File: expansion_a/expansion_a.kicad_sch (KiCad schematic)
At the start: 3 parts, among them J101 Conn_01x08, U101 74HC373, U102 74HC595

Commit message: Expander Final II
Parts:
- U102: footprint Package_SO:STC_SOP-16_3.9x9.9mm_P1.27mm -> Package_SO:SOIC-16W_5.3x10.2mm_P1.27mm; LCSC C18164493 -> C5947
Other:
- sheet Output 1 ports: added set(3V3); removed set(+5V)
- sheet Output 2 ports: added set(3V3); removed set(+5V)
- sheet Output 3 ports: added set(3V3); removed set(+5V)
- sheet Output 4 ports: added set(3V3); removed set(+5V)
- sheet Output 5 ports: added set(3V3); removed set(+5V)
- sheet Output 6 ports: added set(3V3); removed set(+5V)
- sheet Output 7 ports: added set(3V3); removed set(+5V)
- sheet Output 8 ports: added set(3V3); removed set(+5V)
- title: (none) -> Expansion Board A
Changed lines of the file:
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@@
 	(generator_version "8.0")
 	(paper "A4")
+	(title_block
+		(title "Expansion Board A")
+		(date "2025-01-01")
+		(rev "1")
+	)
 	(junction
 		(at 247.65 25.4)
@@
 			)
 		)
-		(property "Footprint" "Package_SO:STC_SOP-16_3.9x9.9mm_P1.27mm"
+		(property "Footprint" "Package_SO:SOIC-16W_5.3x10.2mm_P1.27mm"
 			(at 160.02 71.12 0)
 			(effects
@@
 			)
 		)
-		(property "LCSC" "C18164493"
+		(property "LCSC" "C5947"
 			(at 160.02 71.12 0)
 			(effects
@@
 			)
 		)
-		(pin "set(+5V)" passive
-			(at 210.82 58.42 180)
+		(pin "output" passive
+			(at 223.52 60.96 0)
 			(effects
 				(font
 					(size 1.27 1.27)
 				)
-				(justify left)
+				(justify right)
 			)
 		)
-		(pin "output" passive
-			(at 223.52 60.96 0)
+		(pin "GND" passive
+			(at 210.82 63.5 180)
 			(effects
 				(font
 					(size 1.27 1.27)
 				)
-				(justify right)
+				(justify left)
 			)
 		)
-		(pin "GND" passive
-			(at 210.82 63.5 180)
+		(pin "set(3V3)" passive
+			(at 210.82 58.42 180)
 			(effects
 				(font
@@
 			)
 		)
-		(pin "set(+5V)" passive
-			(at 257.81 33.02 180)
+		(pin "output" passive
+			(at 270.51 35.56 0)
 			(effects
 				(font
 					(size 1.27 1.27)
 				)
-				(justify left)
+				(justify right)
 			)
 		)
-		(pin "output" passive
-			(at 270.51 35.56 0)
+		(pin "GND" passive
+			(at 257.81 38.1 180)
 			(effects
 				(font
 					(size 1.27 1.27)
 				)
-				(justify right)
+				(justify left)
 			)
 		)
-		(pin "GND" passive
-			(at 257.81 38.1 180)
+		(pin "set(3V3)" passive
+			(at 257.81 33.02 180)
 			(effects
 				(font
@@
 			)
 		)
-		(pin "set(+5V)" passive
-			(at 210.82 33.02 180)
+		(pin "output" passive
+			(at 223.52 35.56 0)
 			(effects
 				(font
 					(size 1.27 1.27)
 				)
-				(justify left)
+				(justify right)
 			)
 		)
-		(pin "output" passive
-			(at 223.52 35.56 0)
+		(pin "GND" passive
+			(at 210.82 38.1 180)
 			(effects
 				(font
 					(size 1.27 1.27)
 				)
-				(justify right)
+				(justify left)
 			)
 		)
-		(pin "GND" passive
-			(at 210.82 38.1 180)
+		(pin "set(3V3)" passive
+			(at 210.82 33.02 180)
 			(effects
 				(font
@@
 			)
 		)
-		(pin "set(+5V)" passive
-			(at 257.81 58.42 180)
+		(pin "output" passive
+			(at 270.51 60.96 0)
 			(effects
 				(font
 					(size 1.27 1.27)
 				)
-				(justify left)
+				(justify right)
 			)
 		)
-		(pin "output" passive
-			(at 270.51 60.96 0)
+		(pin "GND" passive
+			(at 257.81 63.5 180)
 			(effects
 				(font
 					(size 1.27 1.27)
 				)
-				(justify right)
+				(justify left)
 			)
 		)
-		(pin "GND" passive
-			(at 257.81 63.5 180)
+		(pin "set(3V3)" passive
+			(at 257.81 58.42 180)
 			(effects
 				(font
@@
 			)
 		)
-		(pin "set(+5V)" passive
-			(at 210.82 82.55 180)
+		(pin "output" passive
+			(at 223.52 85.09 0)
 			(effects
 				(font
 					(size 1.27 1.27)
 				)
-				(justify left)
+				(justify right)
 			)
 		)
-		(pin "output" passive
-			(at 223.52 85.09 0)
+		(pin "GND" passive
+			(at 210.82 87.63 180)
 			(effects
 				(font
 					(size 1.27 1.27)
 				)
-				(justify right)
+				(justify left)
 			)
 		)
-		(pin "GND" passive
-			(at 210.82 87.63 180)
+		(pin "set(3V3)" passive
+			(at 210.82 82.55 180)
 			(effects
 				(font
@@
 			)
 		)
-		(pin "set(+5V)" passive
-			(at 257.81 107.95 180)
+		(pin "output" passive
+			(at 270.51 110.49 0)
 			(effects
 				(font
 					(size 1.27 1.27)
 				)
-				(justify left)
+				(justify right)
 			)
 		)
-		(pin "output" passive
-			(at 270.51 110.49 0)
+		(pin "GND" passive
+			(at 257.81 113.03 180)
 			(effects
 				(font
 					(size 1.27 1.27)
 				)
-				(justify right)
+				(justify left)
 			)
 		)
-		(pin "GND" passive
-			(at 257.81 113.03 180)
+		(pin "set(3V3)" passive
+			(at 257.81 107.95 180)
 			(effects
 				(font
@@
 			)
 		)
-		(pin "set(+5V)" passive
-			(at 210.82 107.95 180)
+		(pin "output" passive
+			(at 223.52 110.49 0)
 			(effects
 				(font
 					(size 1.27 1.27)
 				)
-				(justify left)
+				(justify right)
 			)
 		)
-		(pin "output" passive
-			(at 223.52 110.49 0)
+		(pin "GND" passive
+			(at 210.82 113.03 180)
 			(effects
 				(font
 					(size 1.27 1.27)
 				)
-				(justify right)
+				(justify left)
 			)
 		)
-		(pin "GND" passive
-			(at 210.82 113.03 180)
+		(pin "set(3V3)" passive
+			(at 210.82 107.95 180)
 			(effects
 				(font
@@
 			)
 		)
-		(pin "set(+5V)" passive
-			(at 257.81 82.55 180)
+		(pin "output" passive
+			(at 270.51 85.09 0)
 			(effects
 				(font
 					(size 1.27 1.27)
 				)
-				(justify left)
+				(justify right)
 			)
 		)
-		(pin "output" passive
-			(at 270.51 85.09 0)
+		(pin "GND" passive
+			(at 257.81 87.63 180)
 			(effects
 				(font
 					(size 1.27 1.27)
 				)
-				(justify right)
+				(justify left)
 			)
 		)
-		(pin "GND" passive
-			(at 257.81 87.63 180)
+		(pin "set(3V3)" passive
+			(at 257.81 82.55 180)
 			(effects
 				(font

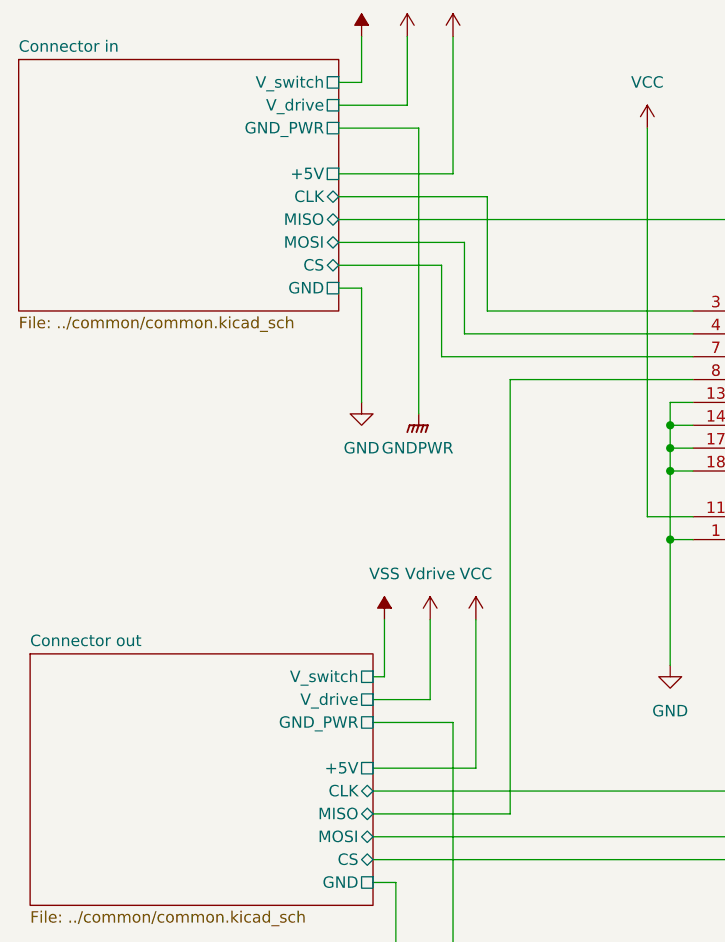
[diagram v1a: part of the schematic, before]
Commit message: Rename common "+5V" to "3V3"
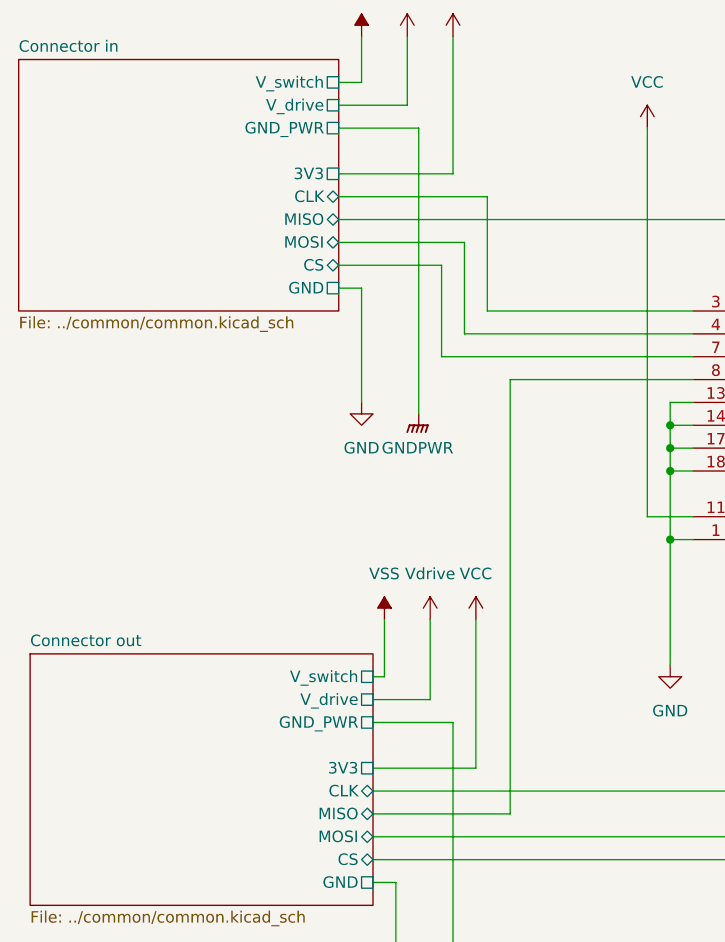
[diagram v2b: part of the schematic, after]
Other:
- sheet Connector in ports: added 3V3; removed +5V
- sheet Connector out ports: added 3V3; removed +5V
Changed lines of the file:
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@@
-			)
-		)
-		(pin "+5V" passive
-			(at 50.8 53.34 0)
-			(effects
-				(font
-					(size 1.27 1.27)
-				)
-				(justify right)
 			)
 		)
@@
 		(pin "CS" bidirectional
 			(at 50.8 63.5 0)
+			(effects
+				(font
+					(size 1.27 1.27)
+				)
+				(justify right)
+			)
+		)
+		(pin "3V3" passive
+			(at 50.8 53.34 0)
 			(effects
 				(font
@@
 			)
 		)
-		(pin "+5V" passive
-			(at 54.61 119.38 0)
-			(effects
-				(font
-					(size 1.27 1.27)
-				)
-				(justify right)
-			)
-		)
 		(pin "V_switch" passive
 			(at 54.61 109.22 0)
@@
 			(effects
 				(font
+					(size 1.27 1.27)
+				)
+				(justify right)
+			)
+		)
+		(pin "3V3" passive
+			(at 54.61 119.38 0)
+			(effects
+				(font

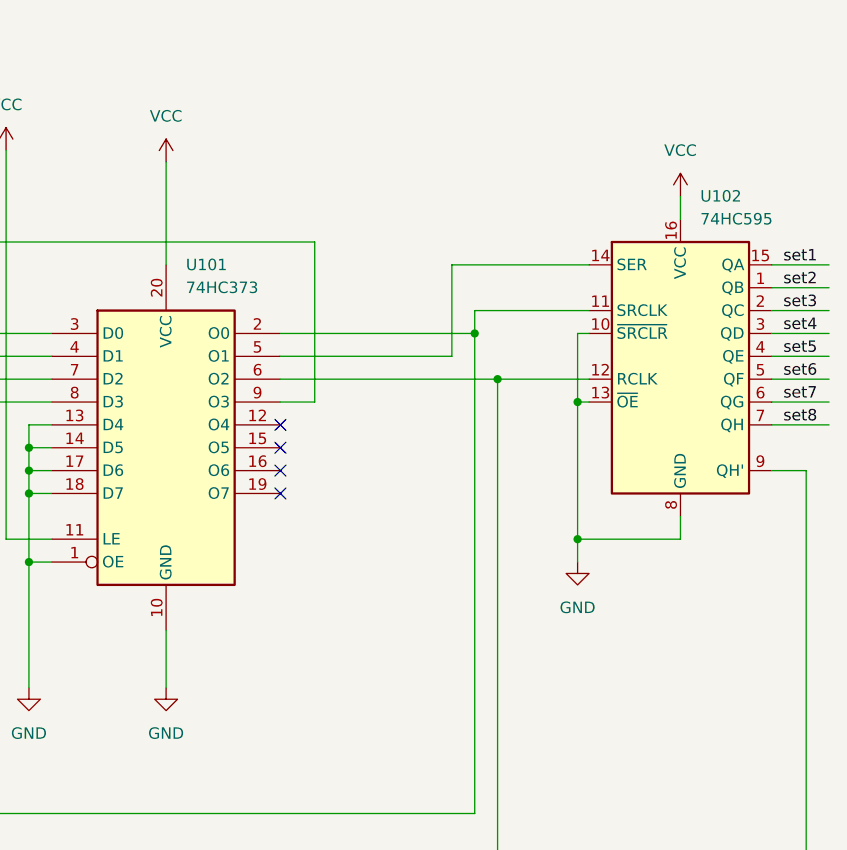
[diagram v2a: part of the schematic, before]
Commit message: Add capacitors for ic
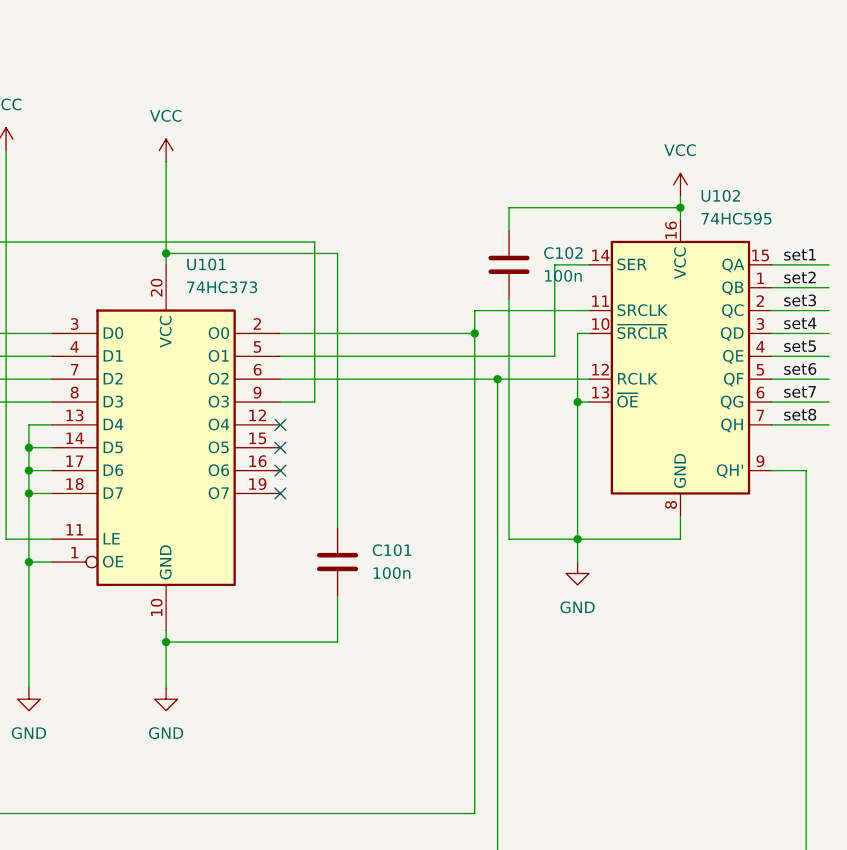
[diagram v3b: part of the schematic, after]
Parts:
- added C101, C102: 100n, Capacitor_SMD:C_0805_2012Metric, symbol Device:C
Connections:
- net GND: now also C101.2, C102.2
- net VCC: now also C101.1, C102.1
